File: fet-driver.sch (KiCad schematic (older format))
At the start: 32 parts, among them Q13 AO3401, Q22 AO3401, Q23 AO3401, Q24 AO3401, Q25 AO3401, Q26 AO3401, Q27 AO3401, Q28 AO3401

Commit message: Switched to new kicad libraries
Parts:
- C16, C17, C24, C25, C26, C27, C37, C38: symbol device:C -> dotmatrix_64x48-rescue:C-device
- Q13, Q22, Q23, Q24, Q25, Q26, Q27, Q28: symbol device:Q_PMOS_GSD -> dotmatrix_64x48-rescue:Q_PMOS_GSD-device
- R106, R107, R108, R109, R110, R111, R112, R113, R90, R91, R92, R93, R94, R95, R96, R97: symbol device:R -> dotmatrix_64x48-rescue:R-device
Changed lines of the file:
@@
 	4400 3800 4400 3750
 $Comp
-L device:Q_PMOS_GSD Q13
+L dotmatrix_64x48-rescue:Q_PMOS_GSD-device Q13
 U 1 1 58170F54
 P 4300 1300
@@
 	4400 5350 4400 5300
 $Comp
-L device:R R90
+L dotmatrix_64x48-rescue:R-device R90
 U 1 1 581715D9
 P 3450 1300
@@
 $EndComp
 $Comp
-L device:R R91
+L dotmatrix_64x48-rescue:R-device R91
 U 1 1 581716D7
 P 3450 2050
@@
 $EndComp
 $Comp
-L device:R R92
+L dotmatrix_64x48-rescue:R-device R92
 U 1 1 58171711
 P 3450 2800
@@
 $EndComp
 $Comp
-L device:R R93
+L dotmatrix_64x48-rescue:R-device R93
 U 1 1 58171776
 P 3450 3550
@@
 $EndComp
 $Comp
-L device:R R94
+L dotmatrix_64x48-rescue:R-device R94
 U 1 1 58171B04
 P 3450 4350
@@
 $EndComp
 $Comp
-L device:R R95
+L dotmatrix_64x48-rescue:R-device R95
 U 1 1 58171B0A
 P 3450 5100
@@
 $EndComp
 $Comp
-L device:R R96
+L dotmatrix_64x48-rescue:R-device R96
 U 1 1 58171B10
 P 3450 5850
@@
 $EndComp
 $Comp
-L device:R R97
+L dotmatrix_64x48-rescue:R-device R97
 U 1 1 58171B16
 P 3450 6600
@@
 $EndComp
 $Comp
-L device:R R110
+L dotmatrix_64x48-rescue:R-device R110
 U 1 1 58171C74
 P 5500 4750
@@
 Connection ~ 4700 4600
 $Comp
-L device:R R111
+L dotmatrix_64x48-rescue:R-device R111
 U 1 1 58172045
 P 5500 5500
@@
 	5350 5500 4700 5500
 $Comp
-L device:R R112
+L dotmatrix_64x48-rescue:R-device R112
 U 1 1 581720DE
 P 5500 6250
@@
 	5350 6250 4700 6250
 $Comp
-L device:R R113
+L dotmatrix_64x48-rescue:R-device R113
 U 1 1 581721A0
 P 5500 7000
@@
 	5350 7000 4700 7000
 $Comp
-L device:R R106
+L dotmatrix_64x48-rescue:R-device R106
 U 1 1 5817233D
 P 5500 1700
@@
 	5350 1700 4700 1700
 $Comp
-L device:R R107
+L dotmatrix_64x48-rescue:R-device R107
 U 1 1 58172888
 P 5500 2450
@@
 	5350 2450 4700 2450
 $Comp
-L device:R R108
+L dotmatrix_64x48-rescue:R-device R108
 U 1 1 5817296B
 P 5500 3200
@@
 	5350 3200 4700 3200
 $Comp
-L device:R R109
+L dotmatrix_64x48-rescue:R-device R109
 U 1 1 58172A3B
 P 5500 3950
@@
 	5350 3950 4700 3950
 $Comp
-L device:Q_PMOS_GSD Q22
+L dotmatrix_64x48-rescue:Q_PMOS_GSD-device Q22
 U 1 1 58185931
 P 4300 2050
@@
 $EndComp
 $Comp
-L device:Q_PMOS_GSD Q23
+L dotmatrix_64x48-rescue:Q_PMOS_GSD-device Q23
 U 1 1 58185A11
 P 4300 2800
@@
 $EndComp
 $Comp
-L device:Q_PMOS_GSD Q24
+L dotmatrix_64x48-rescue:Q_PMOS_GSD-device Q24
 U 1 1 58185B83
 P 4300 3550
@@
 $EndComp
 $Comp
-L device:Q_PMOS_GSD Q25
+L dotmatrix_64x48-rescue:Q_PMOS_GSD-device Q25
 U 1 1 58185CB1
 P 4300 4350
@@
 $EndComp
 $Comp
-L device:Q_PMOS_GSD Q26
+L dotmatrix_64x48-rescue:Q_PMOS_GSD-device Q26
 U 1 1 58185D8F
 P 4300 5100
@@
 $EndComp
 $Comp
-L device:Q_PMOS_GSD Q27
+L dotmatrix_64x48-rescue:Q_PMOS_GSD-device Q27
 U 1 1 58185F92
 P 4300 5850
@@
 $EndComp
 $Comp
-L device:Q_PMOS_GSD Q28
+L dotmatrix_64x48-rescue:Q_PMOS_GSD-device Q28
 U 1 1 5818602B
 P 4300 6600
@@
 LEDVDD
 $Comp
-L device:C C16
+L dotmatrix_64x48-rescue:C-device C16
 U 1 1 58185CB0
 P 5800 1400
@@
 LEDVDD
 $Comp
-L device:C C17
+L dotmatrix_64x48-rescue:C-device C17
 U 1 1 581864C9
 P 5800 2150
@@
 LEDVDD
 $Comp
-L device:C C24
+L dotmatrix_64x48-rescue:C-device C24
 U 1 1 58186564
 P 5800 2900
@@
 LEDVDD
 $Comp
-L device:C C25
+L dotmatrix_64x48-rescue:C-device C25
 U 1 1 581865F8
 P 5800 3650
@@
 LEDVDD
 $Comp
-L device:C C26
+L dotmatrix_64x48-rescue:C-device C26
 U 1 1 58186806
 P 5800 4450
@@
 LEDVDD
 $Comp
-L device:C C27
+L dotmatrix_64x48-rescue:C-device C27
 U 1 1 581868F4
 P 5800 5200
@@
 LEDVDD
 $Comp
-L device:C C37
+L dotmatrix_64x48-rescue:C-device C37
 U 1 1 58186B25
 P 5800 5950
@@
 LEDVDD
 $Comp
-L device:C C38
+L dotmatrix_64x48-rescue:C-device C38
 U 1 1 58186DEC
 P 5800 6700
@@
 	3000 6600 3300 6600
 $Comp
-L power:GND #PWR092
+L dotmatrix_64x48-rescue:GND-power #PWR092
 U 1 1 5943CA8A
 P 5800 1700
@@
 $EndComp
 $Comp
-L power:GND #PWR093
+L dotmatrix_64x48-rescue:GND-power #PWR093
 U 1 1 5943CD8E
 P 5800 2450
@@
 $EndComp
 $Comp
-L power:GND #PWR094
+L dotmatrix_64x48-rescue:GND-power #PWR094
 U 1 1 5943CDBC
 P 5800 3200
@@
 $EndComp
 $Comp
-L power:GND #PWR095
+L dotmatrix_64x48-rescue:GND-power #PWR095
 U 1 1 5943CFF2
 P 5800 3950
@@
 $EndComp
 $Comp
-L power:GND #PWR096
+L dotmatrix_64x48-rescue:GND-power #PWR096
 U 1 1 5943D1B0
 P 5800 4750
@@
 $EndComp
 $Comp
-L power:GND #PWR097
+L dotmatrix_64x48-rescue:GND-power #PWR097
 U 1 1 5943D1DE
 P 5800 5500
@@
 $EndComp
 $Comp
-L power:GND #PWR098
+L dotmatrix_64x48-rescue:GND-power #PWR098
 U 1 1 5943D414
 P 5800 6250
@@
 $EndComp
 $Comp
-L power:GND #PWR099
+L dotmatrix_64x48-rescue:GND-power #PWR099
 U 1 1 5943D442
 P 5800 7000

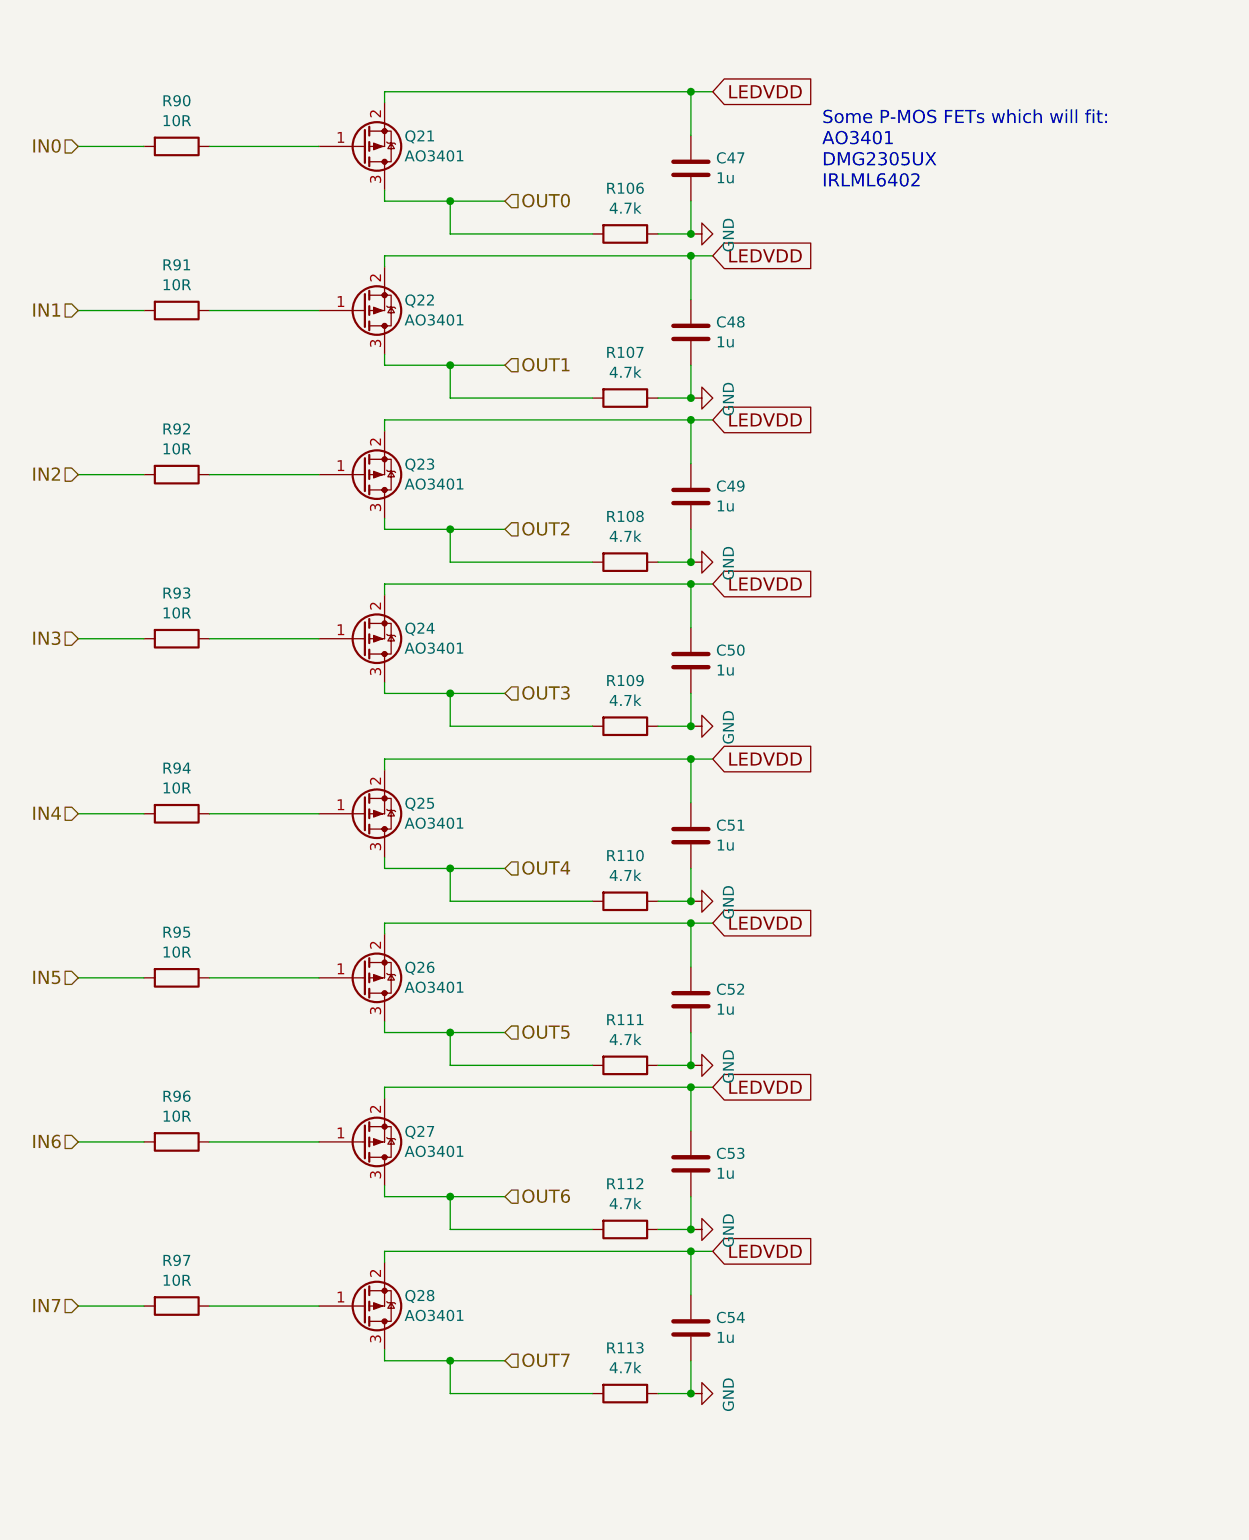
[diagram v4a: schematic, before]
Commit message: Changed footprints from old 4.x's R/C to 5.x's
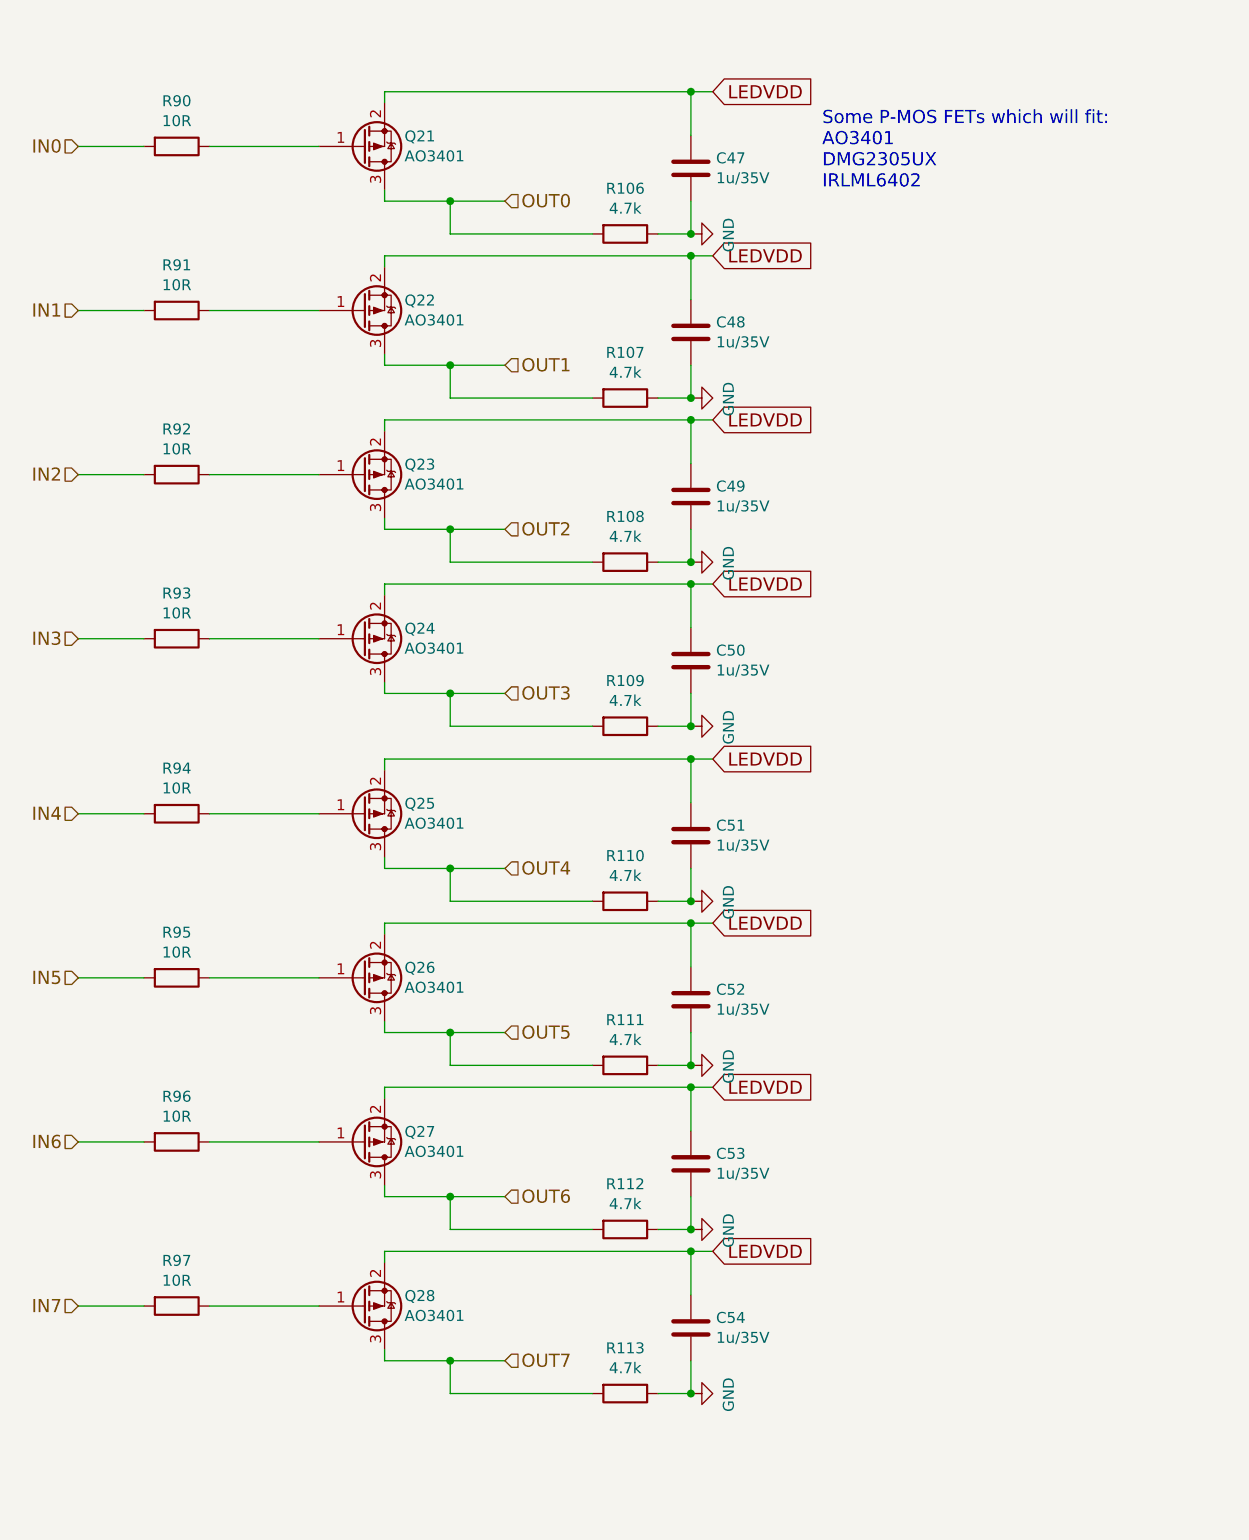
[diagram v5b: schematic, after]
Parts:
- C16, C17, C24, C25, C26, C27, C37, C38: value 1u -> 1u/35V; footprint Capacitors_SMD:C_0603_HandSoldering -> Capacitor_SMD:C_0603_1608Metric_Pad1.05x0.95mm_HandSolder
- R106, R107, R108, R109, R110, R111, R112, R113, R90, R91, R92, R93, R94, R95, R96, R97: footprint Resistors_SMD:R_0603_HandSoldering -> Resistor_SMD:R_0603_1608Metric_Pad1.05x0.95mm_HandSolder
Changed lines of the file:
@@
 F 0 "R90" V 3243 1300 50  0000 C CNN
 F 1 "10R" V 3334 1300 50  0000 C CNN
-F 2 "Resistors_SMD:R_0603_HandSoldering" V 3380 1300 50  0001 C CNN
+F 2 "Resistor_SMD:R_0603_1608Metric_Pad1.05x0.95mm_HandSolder" V 3380 1300 50  0001 C CNN
 F 3 "" H 3450 1300 50  0000 C CNN
 	1    3450 1300
@@
 F 0 "R91" V 3243 2050 50  0000 C CNN
 F 1 "10R" V 3334 2050 50  0000 C CNN
-F 2 "Resistors_SMD:R_0603_HandSoldering" V 3380 2050 50  0001 C CNN
+F 2 "Resistor_SMD:R_0603_1608Metric_Pad1.05x0.95mm_HandSolder" V 3380 2050 50  0001 C CNN
 F 3 "" H 3450 2050 50  0000 C CNN
 	1    3450 2050
@@
 F 0 "R92" V 3243 2800 50  0000 C CNN
 F 1 "10R" V 3334 2800 50  0000 C CNN
-F 2 "Resistors_SMD:R_0603_HandSoldering" V 3380 2800 50  0001 C CNN
+F 2 "Resistor_SMD:R_0603_1608Metric_Pad1.05x0.95mm_HandSolder" V 3380 2800 50  0001 C CNN
 F 3 "" H 3450 2800 50  0000 C CNN
 	1    3450 2800
@@
 F 0 "R93" V 3243 3550 50  0000 C CNN
 F 1 "10R" V 3334 3550 50  0000 C CNN
-F 2 "Resistors_SMD:R_0603_HandSoldering" V 3380 3550 50  0001 C CNN
+F 2 "Resistor_SMD:R_0603_1608Metric_Pad1.05x0.95mm_HandSolder" V 3380 3550 50  0001 C CNN
 F 3 "" H 3450 3550 50  0000 C CNN
 	1    3450 3550
@@
 F 0 "R94" V 3243 4350 50  0000 C CNN
 F 1 "10R" V 3334 4350 50  0000 C CNN
-F 2 "Resistors_SMD:R_0603_HandSoldering" V 3380 4350 50  0001 C CNN
+F 2 "Resistor_SMD:R_0603_1608Metric_Pad1.05x0.95mm_HandSolder" V 3380 4350 50  0001 C CNN
 F 3 "" H 3450 4350 50  0000 C CNN
 	1    3450 4350
@@
 F 0 "R95" V 3243 5100 50  0000 C CNN
 F 1 "10R" V 3334 5100 50  0000 C CNN
-F 2 "Resistors_SMD:R_0603_HandSoldering" V 3380 5100 50  0001 C CNN
+F 2 "Resistor_SMD:R_0603_1608Metric_Pad1.05x0.95mm_HandSolder" V 3380 5100 50  0001 C CNN
 F 3 "" H 3450 5100 50  0000 C CNN
 	1    3450 5100
@@
 F 0 "R96" V 3243 5850 50  0000 C CNN
 F 1 "10R" V 3334 5850 50  0000 C CNN
-F 2 "Resistors_SMD:R_0603_HandSoldering" V 3380 5850 50  0001 C CNN
+F 2 "Resistor_SMD:R_0603_1608Metric_Pad1.05x0.95mm_HandSolder" V 3380 5850 50  0001 C CNN
 F 3 "" H 3450 5850 50  0000 C CNN
 	1    3450 5850
@@
 F 0 "R97" V 3243 6600 50  0000 C CNN
 F 1 "10R" V 3334 6600 50  0000 C CNN
-F 2 "Resistors_SMD:R_0603_HandSoldering" V 3380 6600 50  0001 C CNN
+F 2 "Resistor_SMD:R_0603_1608Metric_Pad1.05x0.95mm_HandSolder" V 3380 6600 50  0001 C CNN
 F 3 "" H 3450 6600 50  0000 C CNN
 	1    3450 6600
@@
 F 0 "R110" V 5293 4750 50  0000 C CNN
 F 1 "4.7k" V 5384 4750 50  0000 C CNN
-F 2 "Resistors_SMD:R_0603_HandSoldering" V 5430 4750 50  0001 C CNN
+F 2 "Resistor_SMD:R_0603_1608Metric_Pad1.05x0.95mm_HandSolder" V 5430 4750 50  0001 C CNN
 F 3 "" H 5500 4750 50  0000 C CNN
 	1    5500 4750
@@
 F 0 "R111" V 5293 5500 50  0000 C CNN
 F 1 "4.7k" V 5384 5500 50  0000 C CNN
-F 2 "Resistors_SMD:R_0603_HandSoldering" V 5430 5500 50  0001 C CNN
+F 2 "Resistor_SMD:R_0603_1608Metric_Pad1.05x0.95mm_HandSolder" V 5430 5500 50  0001 C CNN
 F 3 "" H 5500 5500 50  0000 C CNN
 	1    5500 5500
@@
 F 0 "R112" V 5293 6250 50  0000 C CNN
 F 1 "4.7k" V 5384 6250 50  0000 C CNN
-F 2 "Resistors_SMD:R_0603_HandSoldering" V 5430 6250 50  0001 C CNN
+F 2 "Resistor_SMD:R_0603_1608Metric_Pad1.05x0.95mm_HandSolder" V 5430 6250 50  0001 C CNN
 F 3 "" H 5500 6250 50  0000 C CNN
 	1    5500 6250
@@
 F 0 "R113" V 5293 7000 50  0000 C CNN
 F 1 "4.7k" V 5384 7000 50  0000 C CNN
-F 2 "Resistors_SMD:R_0603_HandSoldering" V 5430 7000 50  0001 C CNN
+F 2 "Resistor_SMD:R_0603_1608Metric_Pad1.05x0.95mm_HandSolder" V 5430 7000 50  0001 C CNN
 F 3 "" H 5500 7000 50  0000 C CNN
 	1    5500 7000
@@
 F 0 "R106" V 5293 1700 50  0000 C CNN
 F 1 "4.7k" V 5384 1700 50  0000 C CNN
-F 2 "Resistors_SMD:R_0603_HandSoldering" V 5430 1700 50  0001 C CNN
+F 2 "Resistor_SMD:R_0603_1608Metric_Pad1.05x0.95mm_HandSolder" V 5430 1700 50  0001 C CNN
 F 3 "" H 5500 1700 50  0000 C CNN
 	1    5500 1700
@@
 F 0 "R107" V 5293 2450 50  0000 C CNN
 F 1 "4.7k" V 5384 2450 50  0000 C CNN
-F 2 "Resistors_SMD:R_0603_HandSoldering" V 5430 2450 50  0001 C CNN
+F 2 "Resistor_SMD:R_0603_1608Metric_Pad1.05x0.95mm_HandSolder" V 5430 2450 50  0001 C CNN
 F 3 "" H 5500 2450 50  0000 C CNN
 	1    5500 2450
@@
 F 0 "R108" V 5293 3200 50  0000 C CNN
 F 1 "4.7k" V 5384 3200 50  0000 C CNN
-F 2 "Resistors_SMD:R_0603_HandSoldering" V 5430 3200 50  0001 C CNN
+F 2 "Resistor_SMD:R_0603_1608Metric_Pad1.05x0.95mm_HandSolder" V 5430 3200 50  0001 C CNN
 F 3 "" H 5500 3200 50  0000 C CNN
 	1    5500 3200
@@
 F 0 "R109" V 5293 3950 50  0000 C CNN
 F 1 "4.7k" V 5384 3950 50  0000 C CNN
-F 2 "Resistors_SMD:R_0603_HandSoldering" V 5430 3950 50  0001 C CNN
+F 2 "Resistor_SMD:R_0603_1608Metric_Pad1.05x0.95mm_HandSolder" V 5430 3950 50  0001 C CNN
 F 3 "" H 5500 3950 50  0000 C CNN
 	1    5500 3950
@@
 AR Path="/58141380/5817D18C/58185CB0" Ref="C47"  Part="1"
 F 0 "C47" H 5915 1446 50  0000 L CNN
-F 1 "1u" H 5915 1355 50  0000 L CNN
-F 2 "Capacitors_SMD:C_0603_HandSoldering" H 5915 1309 50  0001 L CNN
+F 1 "1u/35V" H 5915 1355 50  0000 L CNN
+F 2 "Capacitor_SMD:C_0603_1608Metric_Pad1.05x0.95mm_HandSolder" H 5915 1309 50  0001 L CNN
 F 3 "" H 5800 1400 50  0000 C CNN
 	1    5800 1400
@@
 AR Path="/58141380/5817D18C/581864C9" Ref="C48"  Part="1"
 F 0 "C48" H 5915 2196 50  0000 L CNN
-F 1 "1u" H 5915 2105 50  0000 L CNN
-F 2 "Capacitors_SMD:C_0603_HandSoldering" H 5915 2059 50  0001 L CNN
+F 1 "1u/35V" H 5915 2105 50  0000 L CNN
+F 2 "Capacitor_SMD:C_0603_1608Metric_Pad1.05x0.95mm_HandSolder" H 5915 2059 50  0001 L CNN
 F 3 "" H 5800 2150 50  0000 C CNN
 	1    5800 2150
@@
 AR Path="/58141380/5817D18C/58186564" Ref="C49"  Part="1"
 F 0 "C49" H 5915 2946 50  0000 L CNN
-F 1 "1u" H 5915 2855 50  0000 L CNN
-F 2 "Capacitors_SMD:C_0603_HandSoldering" H 5915 2809 50  0001 L CNN
+F 1 "1u/35V" H 5915 2855 50  0000 L CNN
+F 2 "Capacitor_SMD:C_0603_1608Metric_Pad1.05x0.95mm_HandSolder" H 5915 2809 50  0001 L CNN
 F 3 "" H 5800 2900 50  0000 C CNN
 	1    5800 2900
@@
 AR Path="/58141380/5817D18C/581865F8" Ref="C50"  Part="1"
 F 0 "C50" H 5915 3696 50  0000 L CNN
-F 1 "1u" H 5915 3605 50  0000 L CNN
-F 2 "Capacitors_SMD:C_0603_HandSoldering" H 5915 3559 50  0001 L CNN
+F 1 "1u/35V" H 5915 3605 50  0000 L CNN
+F 2 "Capacitor_SMD:C_0603_1608Metric_Pad1.05x0.95mm_HandSolder" H 5915 3559 50  0001 L CNN
 F 3 "" H 5800 3650 50  0000 C CNN
 	1    5800 3650
@@
 AR Path="/58141380/5817D18C/58186806" Ref="C51"  Part="1"
 F 0 "C51" H 5915 4496 50  0000 L CNN
-F 1 "1u" H 5915 4405 50  0000 L CNN
-F 2 "Capacitors_SMD:C_0603_HandSoldering" H 5915 4359 50  0001 L CNN
+F 1 "1u/35V" H 5915 4405 50  0000 L CNN
+F 2 "Capacitor_SMD:C_0603_1608Metric_Pad1.05x0.95mm_HandSolder" H 5915 4359 50  0001 L CNN
 F 3 "" H 5800 4450 50  0000 C CNN
 	1    5800 4450
@@
 AR Path="/58141380/5817D18C/581868F4" Ref="C52"  Part="1"
 F 0 "C52" H 5915 5246 50  0000 L CNN
-F 1 "1u" H 5915 5155 50  0000 L CNN
-F 2 "Capacitors_SMD:C_0603_HandSoldering" H 5915 5109 50  0001 L CNN
+F 1 "1u/35V" H 5915 5155 50  0000 L CNN
+F 2 "Capacitor_SMD:C_0603_1608Metric_Pad1.05x0.95mm_HandSolder" H 5915 5109 50  0001 L CNN
 F 3 "" H 5800 5200 50  0000 C CNN
 	1    5800 5200
@@
 AR Path="/58141380/5817D18C/58186B25" Ref="C53"  Part="1"
 F 0 "C53" H 5915 5996 50  0000 L CNN
-F 1 "1u" H 5915 5905 50  0000 L CNN
-F 2 "Capacitors_SMD:C_0603_HandSoldering" H 5915 5859 50  0001 L CNN
+F 1 "1u/35V" H 5915 5905 50  0000 L CNN
+F 2 "Capacitor_SMD:C_0603_1608Metric_Pad1.05x0.95mm_HandSolder" H 5915 5859 50  0001 L CNN
 F 3 "" H 5800 5950 50  0000 C CNN
 	1    5800 5950
@@
 AR Path="/58141380/5817D18C/58186DEC" Ref="C54"  Part="1"
 F 0 "C54" H 5915 6746 50  0000 L CNN
-F 1 "1u" H 5915 6655 50  0000 L CNN
-F 2 "Capacitors_SMD:C_0603_HandSoldering" H 5915 6609 50  0001 L CNN
+F 1 "1u/35V" H 5915 6655 50  0000 L CNN
+F 2 "Capacitor_SMD:C_0603_1608Metric_Pad1.05x0.95mm_HandSolder" H 5915 6609 50  0001 L CNN
 F 3 "" H 5800 6700 50  0000 C CNN
 	1    5800 6700
